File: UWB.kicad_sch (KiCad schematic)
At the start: 11 parts, among them U9 DWM3000TR13

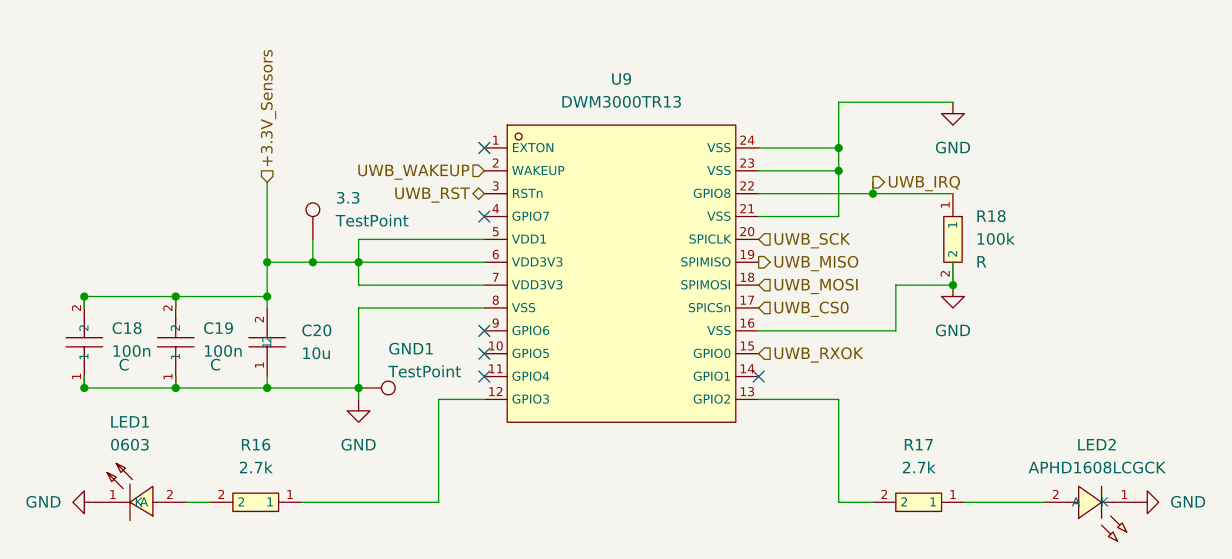
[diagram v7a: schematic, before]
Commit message: KiCad: PCB placement, routing and schematic updates
Wiring of component blocks and sensors + component rearrangement + routing
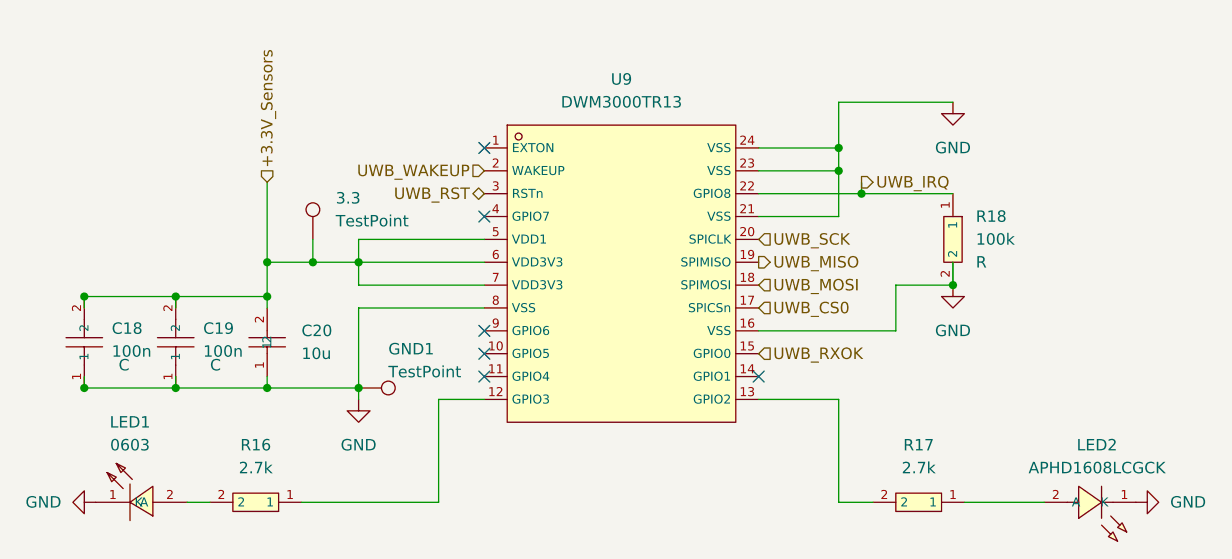
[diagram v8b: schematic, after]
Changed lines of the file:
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@@
 	(paper "A4")
 	(junction
+		(at 167.64 80.01)
+		(diameter 0)
+		(color 0 0 0 0)
+	)
+	(junction
 		(at 81.28 101.6)
 		(diameter 0)
@@
 	)
 	(junction
-		(at 168.91 80.01)
-		(diameter 0)
-		(color 0 0 0 0)
-	)
-	(junction
 		(at 81.28 91.44)
 		(diameter 0)
@@
 	(wire
 		(pts
+			(xy 167.64 80.01) (xy 177.8 80.01)
+		)
+		(stroke
+			(width 0)
+			(type default)
+		)
+	)
+	(wire
+		(pts
 			(xy 165.1 102.87) (xy 165.1 114.3)
 		)
@@
 	(wire
 		(pts
-			(xy 156.21 80.01) (xy 168.91 80.01)
+			(xy 156.21 80.01) (xy 167.64 80.01)
 		)
 		(stroke
@@
 	(wire
 		(pts
-			(xy 168.91 80.01) (xy 177.8 80.01)
-		)
-		(stroke
-			(width 0)
-			(type default)
-		)
-	)
-	(wire
-		(pts
 			(xy 101.6 87.63) (xy 106.68 87.63)
 		)
@@
 	(wire
 		(pts
-			(xy 168.91 78.74) (xy 168.91 80.01)
+			(xy 167.64 78.74) (xy 167.64 80.01)
 		)
 		(stroke
@@
 	(hierarchical_label "UWB_IRQ"
 		(shape output)
-		(at 168.91 78.74 0)
+		(at 167.64 78.74 0)
 		(effects
 			(font
